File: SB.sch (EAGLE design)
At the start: 48 parts, among them IC1 ATMEGA32U4NT-TQFP, IC2 HX711-SOP16L, J2 RJ12, J3 AUDIO-JACK-PJ321, J5 USB-C-16P-16P, K1 HE721C-DIP, Q1 2N7002, Q2 2N7002, Q3 2N3906, SW1 SWITCH-SPDT-4TABSSMT

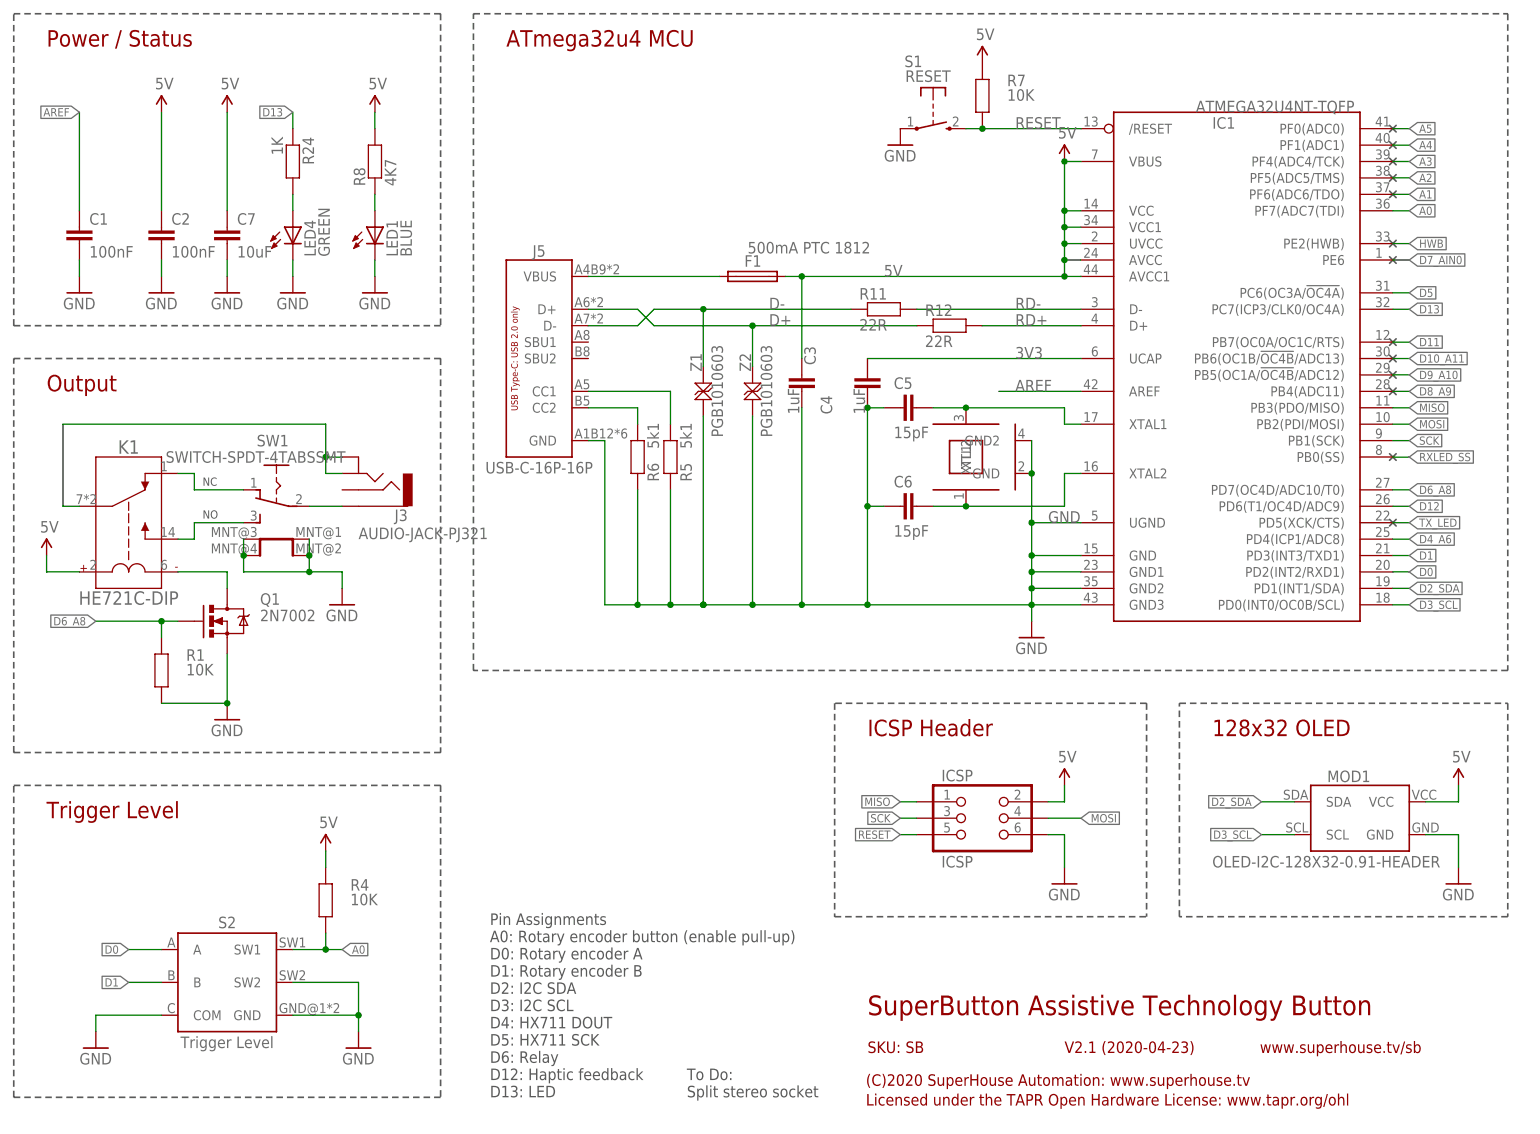
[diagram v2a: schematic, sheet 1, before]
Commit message: Added Tare button and beep stretch switch, still for v2.1 release
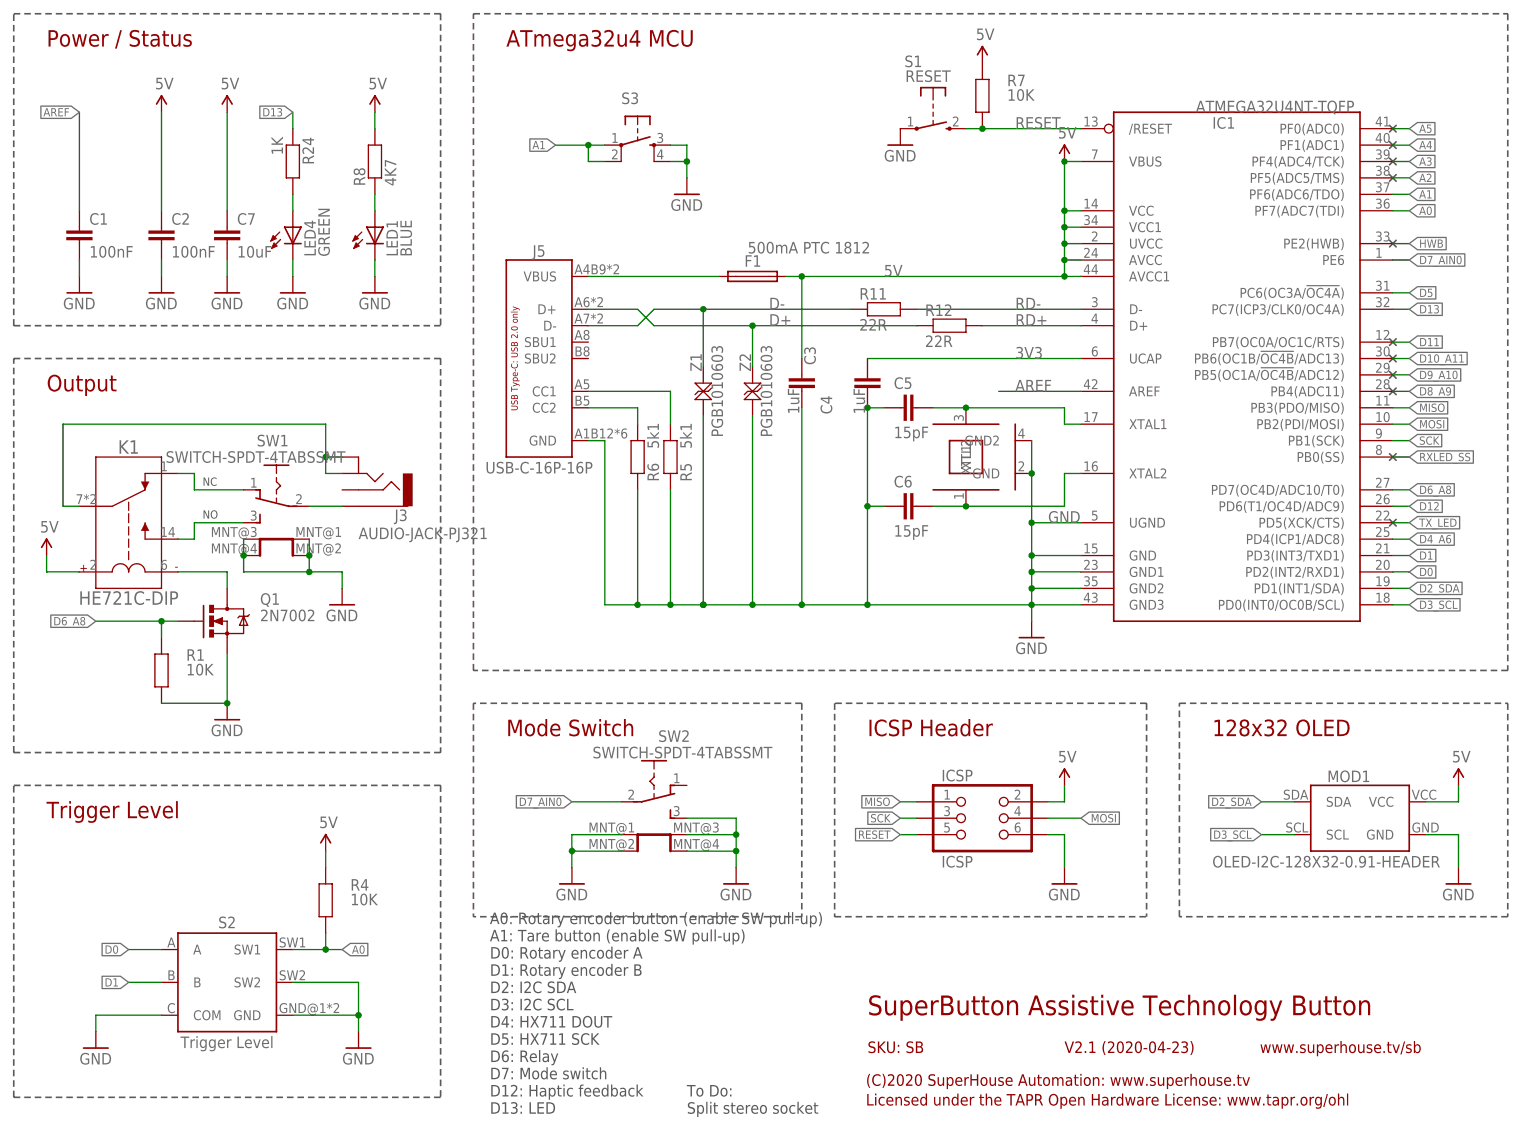
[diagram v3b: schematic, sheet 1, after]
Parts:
- added S3: (no value), SuperHouse-Switches:TAC_SWITCH-PTH-4.5
- added SW2: SWITCH-SPDT-4TABSSMT, SuperHouse-Switches:SWITCH-SPDT-4TABSSMT
- C3, C4: device SuperHouse-DiscreteSemi:CAP0603 -> SuperHouse-DiscreteSemi:CAP0805
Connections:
- net A1: now also S3.1, S3.2
- net D7_AIN0: now also SW2.COM
- net GND: now also S3.3, S3.4, SW2.B, SW2.MNT@1, SW2.MNT@2, SW2.MNT@3, SW2.MNT@4
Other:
- note added: "A0: Rotary encoder button (enable SW pull-up) A1: Tare button (enable SW pull-up) D0: Rotary encoder A D1: Rotary encoder B D2: I2C SDA D3: I2C SCL D4: HX711 DOUT D5: HX711 SCK D6: Relay D7: Mode switch D12: Haptic feedback D13: LED"
- note added: "Mode Switch"
- note removed: "Pin Assignments A0: Rotary encoder button (enable pull-up) D0: Rotary encoder A D1: Rotary encoder B D2: I2C SDA D3: I2C SCL D4: HX711 DOUT D5: HX711 SCK D6: Relay D12: Haptic feedback D13: LED"
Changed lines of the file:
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@@
 <part name="R7" library="SuperHouse-DiscreteSemi" library_urn="urn:adsk.eagle:library:11768461" deviceset="RESISTOR" device="0603" package3d_urn="urn:adsk.eagle:package:11768543/2" value="10K"/>
 <part name="U$1" library="SuperHouse-SupplySymbols" library_urn="urn:adsk.eagle:library:11790503" deviceset="5V" device=""/>
-<part name="C3" library="SuperHouse-DiscreteSemi" library_urn="urn:adsk.eagle:library:11768461" deviceset="CAP" device="0603" package3d_urn="urn:adsk.eagle:package:7066315/6" value="1uF"/>
+<part name="C3" library="SuperHouse-DiscreteSemi" library_urn="urn:adsk.eagle:library:11768461" deviceset="CAP" device="0805" package3d_urn="urn:adsk.eagle:package:7066318/4" value="1uF"/>
 <part name="C1" library="SuperHouse-DiscreteSemi" library_urn="urn:adsk.eagle:library:11768461" deviceset="CAP" device="0603" package3d_urn="urn:adsk.eagle:package:7066315/6" value="100nF"/>
 <part name="GND11" library="SuperHouse-SupplySymbols" library_urn="urn:adsk.eagle:library:11790503" deviceset="GND" device=""/>
@@
 <part name="C5" library="SuperHouse-DiscreteSemi" library_urn="urn:adsk.eagle:library:11768461" deviceset="CAP" device="0603" package3d_urn="urn:adsk.eagle:package:7066315/6" value="15pF"/>
 <part name="C6" library="SuperHouse-DiscreteSemi" library_urn="urn:adsk.eagle:library:11768461" deviceset="CAP" device="0603" package3d_urn="urn:adsk.eagle:package:7066315/6" value="15pF"/>
-<part name="C4" library="SuperHouse-DiscreteSemi" library_urn="urn:adsk.eagle:library:11768461" deviceset="CAP" device="0603" package3d_urn="urn:adsk.eagle:package:7066315/6" value="1uF"/>
+<part name="C4" library="SuperHouse-DiscreteSemi" library_urn="urn:adsk.eagle:library:11768461" deviceset="CAP" device="0805" package3d_urn="urn:adsk.eagle:package:7066318/4" value="1uF"/>
 <part name="XTL1" library="SuperHouse-Oscillators" library_urn="urn:adsk.eagle:library:11786724" deviceset="CRYSTAL-GND" device="3X2" package3d_urn="urn:adsk.eagle:package:7066259/2" value="16MHz"/>
 <part name="GND13" library="SuperHouse-SupplySymbols" library_urn="urn:adsk.eagle:library:11790503" deviceset="GND" device=""/>
@@
 <part name="U$12" library="SuperHouse-SupplySymbols" library_urn="urn:adsk.eagle:library:11790503" deviceset="NC" device=""/>
 <part name="U$13" library="SuperHouse-SupplySymbols" library_urn="urn:adsk.eagle:library:11790503" deviceset="NC" device=""/>
-<part name="U$14" library="SuperHouse-SupplySymbols" library_urn="urn:adsk.eagle:library:11790503" deviceset="NC" device=""/>
 <part name="U$15" library="SuperHouse-SupplySymbols" library_urn="urn:adsk.eagle:library:11790503" deviceset="NC" device=""/>
-<part name="U$16" library="SuperHouse-SupplySymbols" library_urn="urn:adsk.eagle:library:11790503" deviceset="NC" device=""/>
 <part name="U$17" library="SuperHouse-SupplySymbols" library_urn="urn:adsk.eagle:library:11790503" deviceset="NC" device=""/>
 <part name="U$18" library="SuperHouse-SupplySymbols" library_urn="urn:adsk.eagle:library:11790503" deviceset="NC" device=""/>
@@
 <part name="SW1" library="SuperHouse-Switches" library_urn="urn:adsk.eagle:library:11744182" deviceset="SWITCH-SPDT-4TABS" device="SMT" package3d_urn="urn:adsk.eagle:package:7066359/2"/>
 <part name="GND10" library="SuperHouse-SupplySymbols" library_urn="urn:adsk.eagle:library:11790503" deviceset="GND" device=""/>
+<part name="SW2" library="SuperHouse-Switches" library_urn="urn:adsk.eagle:library:11744182" deviceset="SWITCH-SPDT-4TABS" device="SMT" package3d_urn="urn:adsk.eagle:package:7066359/2"/>
+<part name="GND14" library="SuperHouse-SupplySymbols" library_urn="urn:adsk.eagle:library:11790503" deviceset="GND" device=""/>
+<part name="GND16" library="SuperHouse-SupplySymbols" library_urn="urn:adsk.eagle:library:11790503" deviceset="GND" device=""/>
+<part name="S3" library="SuperHouse-Switches" library_urn="urn:adsk.eagle:library:11744182" deviceset="TAC_SWITCH" device="-PTH-4.5" package3d_urn="urn:adsk.eagle:package:7066371/2"/>
+<part name="GND17" library="SuperHouse-SupplySymbols" library_urn="urn:adsk.eagle:library:11790503" deviceset="GND" device=""/>
 </parts>
 <sheets>
@@
 <wire x1="241.3" y1="73.66" x2="81.28" y2="73.66" width="0.254" layer="97" style="longdash"/>
 <wire x1="81.28" y1="73.66" x2="81.28" y2="175.26" width="0.254" layer="97" style="longdash"/>
-<text x="83.82" y="7.62" size="1.778" layer="97">Pin Assignments
-A0: Rotary encoder button (enable pull-up)
+<text x="83.82" y="5.08" size="1.778" layer="97">A0: Rotary encoder button (enable SW pull-up)
+A1: Tare button (enable SW pull-up)
 D0: Rotary encoder A
 D1: Rotary encoder B
@@
 D5: HX711 SCK
 D6: Relay
+D7: Mode switch
 D12: Haptic feedback
 D13: LED</text>
 <text x="39.37" y="97.155" size="1.27" layer="97">NO</text>
 <text x="39.37" y="102.235" size="1.27" layer="97">NC</text>
-<text x="114.3" y="7.62" size="1.778" layer="97">To Do:
+<text x="114.3" y="5.08" size="1.778" layer="97">To Do:
 Split stereo socket</text>
+<wire x1="81.28" y1="68.58" x2="81.28" y2="35.56" width="0.254" layer="97" style="longdash"/>
+<wire x1="132.08" y1="68.58" x2="132.08" y2="35.56" width="0.254" layer="97" style="longdash"/>
+<wire x1="132.08" y1="68.58" x2="81.28" y2="68.58" width="0.254" layer="97" style="longdash"/>
+<wire x1="132.08" y1="35.56" x2="81.28" y2="35.56" width="0.254" layer="97" style="longdash"/>
+<text x="86.36" y="63.5" size="2.54" layer="94" ratio="12">Mode Switch</text>
 </plain>
 <instances>
@@
 <instance part="U$12" gate="G$1" x="223.52" y="152.4" smashed="yes"/>
 <instance part="U$13" gate="G$1" x="223.52" y="149.86" smashed="yes"/>
-<instance part="U$14" gate="G$1" x="223.52" y="147.32" smashed="yes"/>
 <instance part="U$15" gate="G$1" x="223.52" y="139.7" smashed="yes"/>
-<instance part="U$16" gate="G$1" x="223.52" y="137.16" smashed="yes"/>
 <instance part="U$17" gate="G$1" x="223.52" y="124.46" smashed="yes"/>
 <instance part="U$18" gate="G$1" x="223.52" y="121.92" smashed="yes"/>
@@
 <attribute name="VALUE" x="58.42" y="81.28" size="1.778" layer="96"/>
 </instance>
+<instance part="SW2" gate="G$1" x="109.22" y="53.34" smashed="yes">
+<attribute name="VALUE" x="99.695" y="60.07" size="1.778" layer="96"/>
+<attribute name="PART" x="109.855" y="62.61" size="1.778" layer="95"/>
+</instance>
+<instance part="GND14" gate="1" x="121.92" y="40.64" smashed="yes">
+<attribute name="VALUE" x="119.38" y="38.1" size="1.778" layer="96"/>
+</instance>
+<instance part="GND16" gate="1" x="96.52" y="40.64" smashed="yes">
+<attribute name="VALUE" x="93.98" y="38.1" size="1.778" layer="96"/>
+</instance>
+<instance part="S3" gate="S" x="106.68" y="154.94" smashed="yes">
+<attribute name="NAME" x="104.14" y="161.29" size="1.778" layer="95"/>
+<attribute name="VALUE" x="104.14" y="148.59" size="1.778" layer="96"/>
+</instance>
+<instance part="GND17" gate="1" x="114.3" y="147.32" smashed="yes">
+<attribute name="VALUE" x="111.76" y="144.78" size="1.778" layer="96"/>
+</instance>
 </instances>
 <busses>
@@
 <pinref part="IC1" gate="G$1" pin="PF6(ADC6/TDO)"/>
 <label x="226.06" y="147.32" size="1.27" layer="95" xref="yes"/>
+</segment>
+<segment>
+<pinref part="S3" gate="S" pin="2"/>
+<wire x1="101.6" y1="152.4" x2="99.06" y2="152.4" width="0.1524" layer="91"/>
+<wire x1="99.06" y1="152.4" x2="99.06" y2="154.94" width="0.1524" layer="91"/>
+<pinref part="S3" gate="S" pin="1"/>
+<wire x1="99.06" y1="154.94" x2="101.6" y2="154.94" width="0.1524" layer="91"/>
+<wire x1="99.06" y1="154.94" x2="93.98" y2="154.94" width="0.1524" layer="91"/>
+<junction x="99.06" y="154.94"/>
+<label x="93.98" y="154.94" size="1.27" layer="95" rot="R180" xref="yes"/>
 </segment>
 </net>
@@
 <junction x="55.88" y="88.9"/>
 </segment>
+<segment>
+<pinref part="SW2" gate="G$1" pin="MNT@2"/>
+<wire x1="104.14" y1="45.72" x2="96.52" y2="45.72" width="0.1524" layer="91"/>
+<pinref part="GND16" gate="1" pin="GND"/>
+<wire x1="96.52" y1="45.72" x2="96.52" y2="43.18" width="0.1524" layer="91"/>
+<wire x1="96.52" y1="45.72" x2="96.52" y2="48.26" width="0.1524" layer="91"/>
+<junction x="96.52" y="45.72"/>
+<pinref part="SW2" gate="G$1" pin="MNT@1"/>
+<wire x1="96.52" y1="48.26" x2="104.14" y2="48.26" width="0.1524" layer="91"/>
+</segment>
+<segment>
+<pinref part="SW2" gate="G$1" pin="MNT@4"/>
+<pinref part="GND14" gate="1" pin="GND"/>
+<wire x1="114.3" y1="45.72" x2="121.92" y2="45.72" width="0.1524" layer="91"/>
+<wire x1="121.92" y1="45.72" x2="121.92" y2="43.18" width="0.1524" layer="91"/>
+<pinref part="SW2" gate="G$1" pin="MNT@3"/>
+<wire x1="114.3" y1="48.26" x2="121.92" y2="48.26" width="0.1524" layer="91"/>
+<wire x1="121.92" y1="48.26" x2="121.92" y2="45.72" width="0.1524" layer="91"/>
+<junction x="121.92" y="45.72"/>
+<pinref part="SW2" gate="G$1" pin="B"/>
+<wire x1="114.3" y1="50.8" x2="121.92" y2="50.8" width="0.1524" layer="91"/>
+<wire x1="121.92" y1="50.8" x2="121.92" y2="48.26" width="0.1524" layer="91"/>
+<junction x="121.92" y="48.26"/>
+</segment>
+<segment>
+<pinref part="S3" gate="S" pin="4"/>
+<pinref part="GND17" gate="1" pin="GND"/>
+<wire x1="111.76" y1="152.4" x2="114.3" y2="152.4" width="0.1524" layer="91"/>
+<wire x1="114.3" y1="152.4" x2="114.3" y2="149.86" width="0.1524" layer="91"/>
+<pinref part="S3" gate="S" pin="3"/>
+<wire x1="111.76" y1="154.94" x2="114.3" y2="154.94" width="0.1524" layer="91"/>
+<wire x1="114.3" y1="154.94" x2="114.3" y2="152.4" width="0.1524" layer="91"/>
+<junction x="114.3" y="152.4"/>
+</segment>
 </net>
 <net name="RESET" class="0">
@@
 <label x="226.06" y="137.16" size="1.27" layer="95" xref="yes"/>
 </segment>
-</net>
+<segment>
+<pinref part="SW2" gate="G$1" pin="COM"/>
+<wire x1="104.14" y1="53.34" x2="96.52" y2="53.34" width="0.1524" layer="91"/>
+<label x="96.52" y="53.34" size="1.27" layer="95" rot="R180" xref="yes"/>
+</segment>
+</net>
